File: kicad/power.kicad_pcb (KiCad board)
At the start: 2 copper layers, 53.8 x 22.9 mm, 27 parts, among them P1 CONN_6, U1 TC54VC3002ECB713, U2 TC54VC3002ECB713, U3 TC54VC3002ECB713, U4 AOZ1280, U5 NMOS, U6 PMOS, U7 NMOS

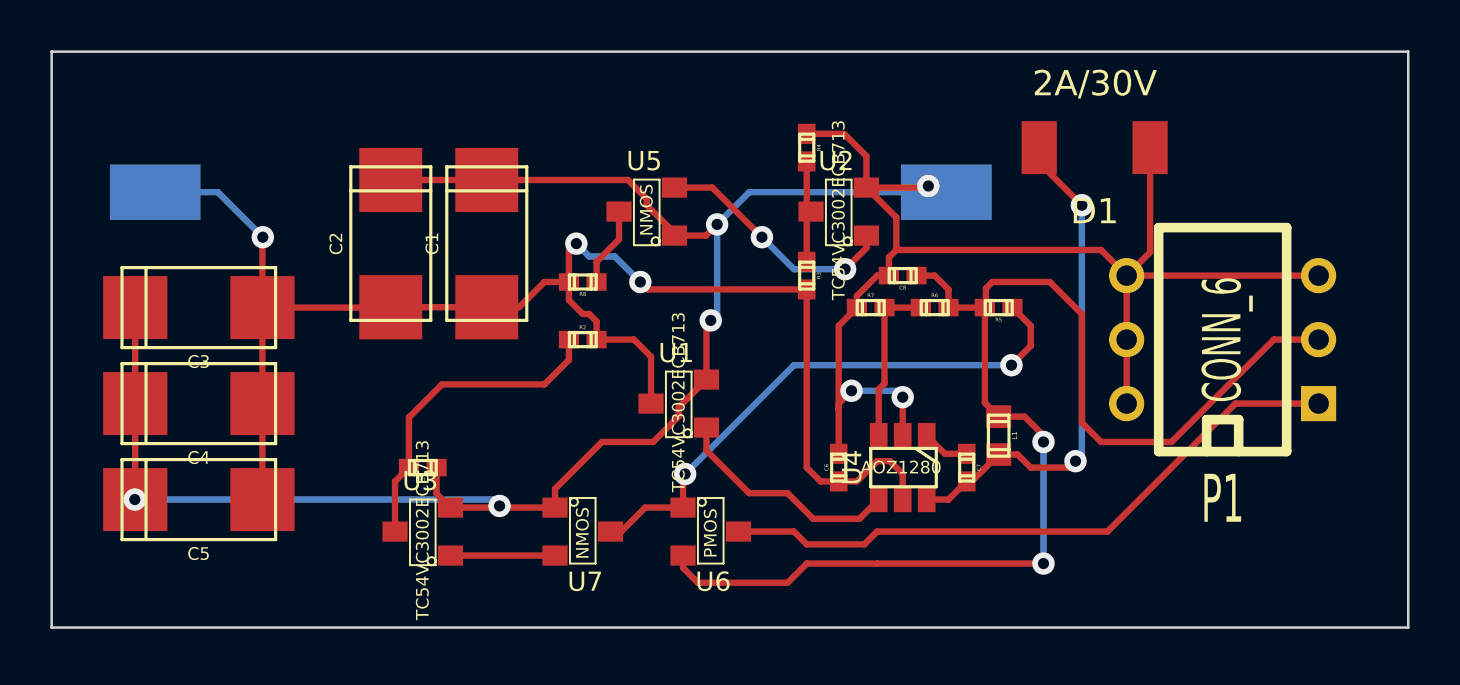
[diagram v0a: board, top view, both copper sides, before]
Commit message: Minor updates to power schematic and board
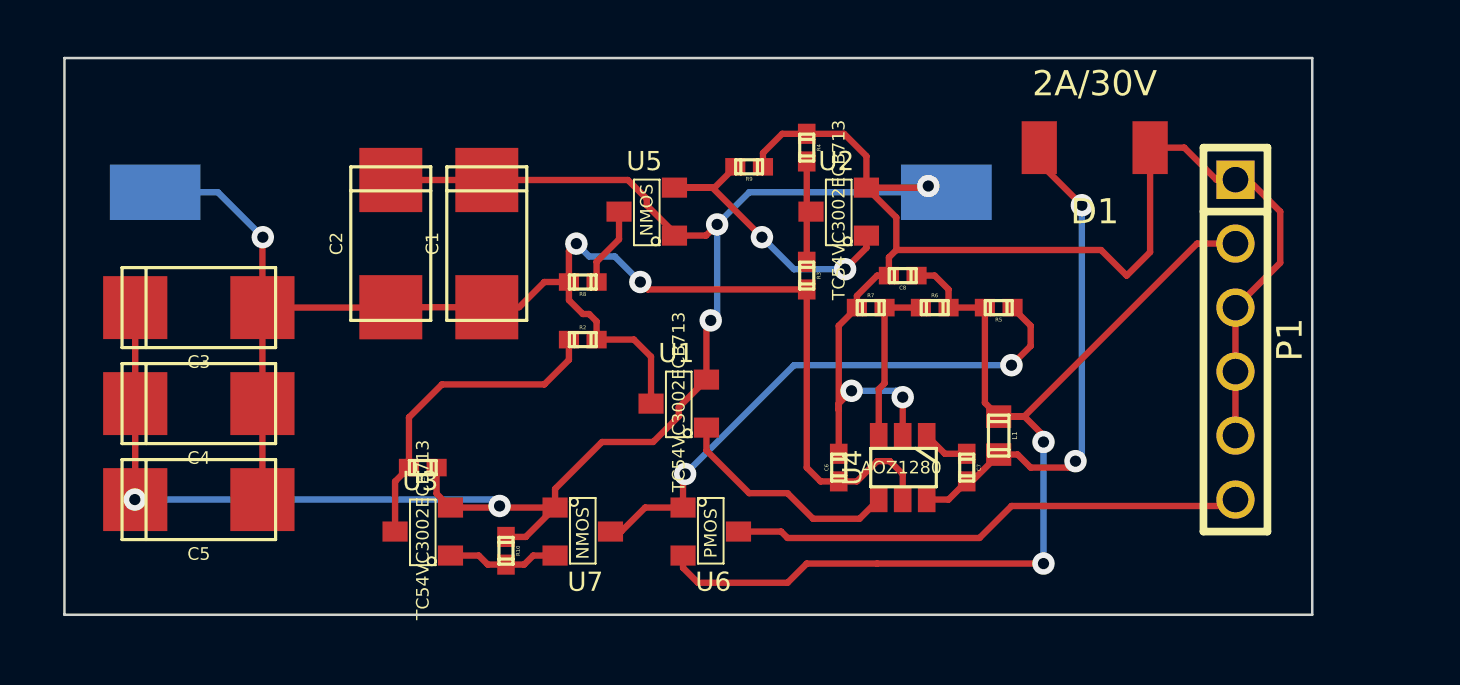
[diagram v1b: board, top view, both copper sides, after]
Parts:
- added R10: 4.7k, c_0402, F.Cu at (214.1, 148.1)
- added R9: 4.7k, c_0402, F.Cu at (223.8, 132.8)
- P1: footprint DIP-6__300 -> PIN_ARRAY-6X1
- moved P1 0.51 mm to (243.1, 139.7), turned to 270 degrees
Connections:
- P1 pad 1: N-0000012 -> GND
- P1 pad 6: GND -> N-000006
- U6 pad 3: N-0000012 -> N-000006
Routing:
- net N-0000012: track 25.6 -> 0.00 mm
- net N-000006: track 0.00 -> 20.5 mm
- net /VOUT: track 51.7 -> 43.0 mm
- net GND: track 119.1 -> 127.3 mm
- net N-000005: track 9.80 -> 12.6 mm
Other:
- board size 53.8 x 22.9 mm -> 49.5 x 22.1 mm
